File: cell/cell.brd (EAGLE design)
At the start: 35.6 x 48.3 mm, 11 parts

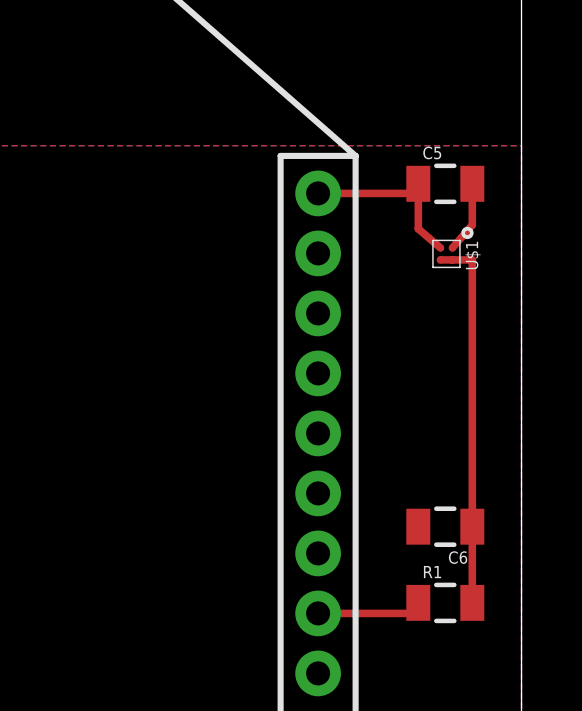
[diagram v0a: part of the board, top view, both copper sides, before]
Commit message: center LMT70 with other chips
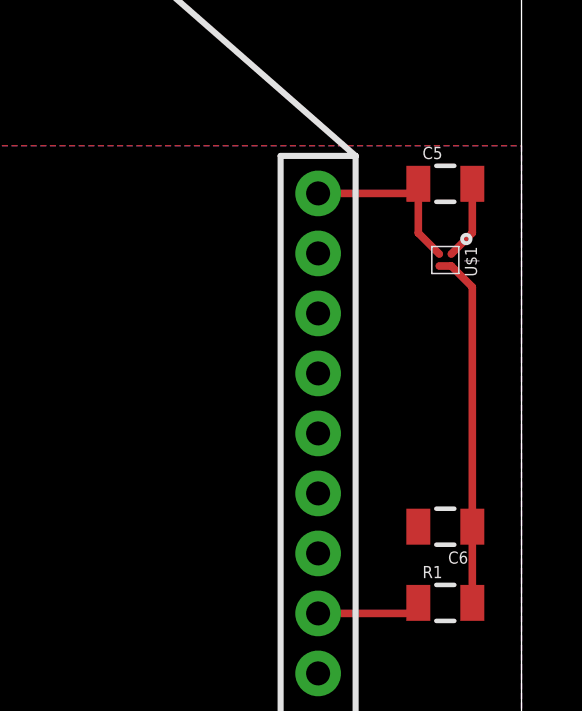
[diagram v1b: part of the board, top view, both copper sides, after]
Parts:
- moved U$1 0.21 mm to (33.0, 30.5)
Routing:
- net N$1: track 12.5 -> 12.0 mm
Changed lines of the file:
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@@
 <element name="C2" library="SparkFun-Capacitors" package="0805" value="1µF" x="25.4" y="6.35"/>
 <element name="XB24" library="hrldcpr" package="XBEE-1" value="XBEE-1XBEE-1" x="17.78" y="12.7"/>
-<element name="U$1" library="lmt40" package="YFP0004" value="LMT40" x="33.0581" y="30.6832" rot="R270"/>
+<element name="U$1" library="lmt40" package="YFP0004" value="LMT40" x="33.02" y="30.48" rot="R270"/>
 </elements>
 <signals>
@@
 <contactref element="XB24" pad="3"/>
 <contactref element="U$1" pad="GND"/>
-<wire x1="33.2581" y1="30.8832" x2="33.92" y2="31.6452" width="0.254" layer="1"/>
-<wire x1="33.92" y1="31.6452" x2="33.92" y2="33.02" width="0.254" layer="1"/>
+<wire x1="33.92" y1="33.02" x2="33.92" y2="31.38" width="0.254" layer="1"/>
+<wire x1="33.92" y1="31.38" x2="33.22" y2="30.68" width="0.254" layer="1"/>
 </signal>
 <signal name="V_BATT">
@@
 <contactref element="U$1" pad="VDD"/>
 <contactref element="U$1" pad="T_ON"/>
-<wire x1="32.8581" y1="30.4832" x2="33.2581" y2="30.4832" width="0.254" layer="1"/>
-<wire x1="33.2581" y1="30.4832" x2="33.92" y2="30.4832" width="0.254" layer="1"/>
-<wire x1="33.92" y1="30.4832" x2="33.92" y2="21.59" width="0.254" layer="1"/>
+<wire x1="32.82" y1="30.28" x2="33.22" y2="30.28" width="0.254" layer="1"/>
+<wire x1="33.22" y1="30.28" x2="33.92" y2="29.58" width="0.254" layer="1"/>
+<wire x1="33.92" y1="29.58" x2="33.92" y2="21.59" width="0.254" layer="1"/>
 </signal>
 <signal name="N$2">
@@
 <wire x1="28.78" y1="32.7" x2="32.12" y2="32.7" width="0.254" layer="1"/>
 <wire x1="32.12" y1="32.7" x2="32.12" y2="33.02" width="0.254" layer="1"/>
-<wire x1="32.8581" y1="30.8832" x2="32.12" y2="31.5182" width="0.254" layer="1"/>
-<wire x1="32.12" y1="31.5182" x2="32.12" y2="33.02" width="0.254" layer="1"/>
+<wire x1="32.12" y1="33.02" x2="32.12" y2="31.38" width="0.254" layer="1"/>
+<wire x1="32.12" y1="31.38" x2="32.82" y2="30.68" width="0.254" layer="1"/>
 </signal>
 </signals>

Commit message: fix LMT70 naming
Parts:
- U$1: value LMT40 -> LMT70; device lmt40:YFP0004 -> lmt70:YFP0004
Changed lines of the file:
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@@
 <element name="C2" library="SparkFun-Capacitors" package="0805" value="1µF" x="25.4" y="6.35"/>
 <element name="XB24" library="hrldcpr" package="XBEE-1" value="XBEE-1XBEE-1" x="17.78" y="12.7"/>
-<element name="U$1" library="lmt40" package="YFP0004" value="LMT40" x="33.02" y="30.48" rot="R270"/>
+<element name="U$1" library="lmt70" package="YFP0004" value="LMT70" x="33.02" y="30.48" rot="R270"/>
 </elements>
 <signals>

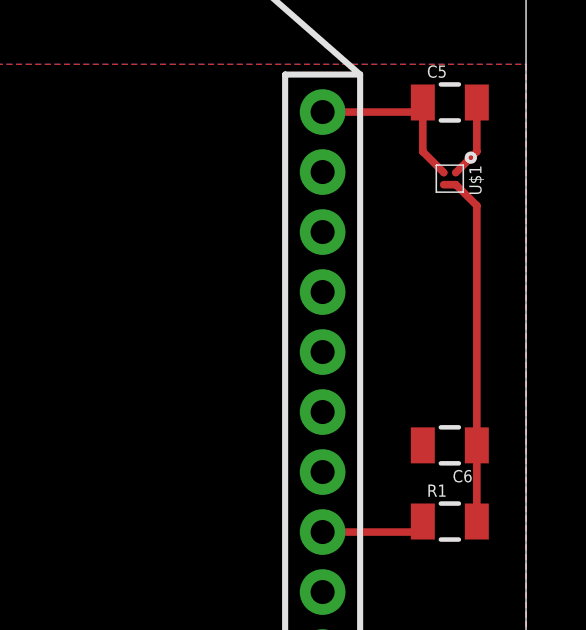
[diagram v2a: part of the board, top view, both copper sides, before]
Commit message: use symmetric traces on BGA chip, to avoid unequal soldering and tension
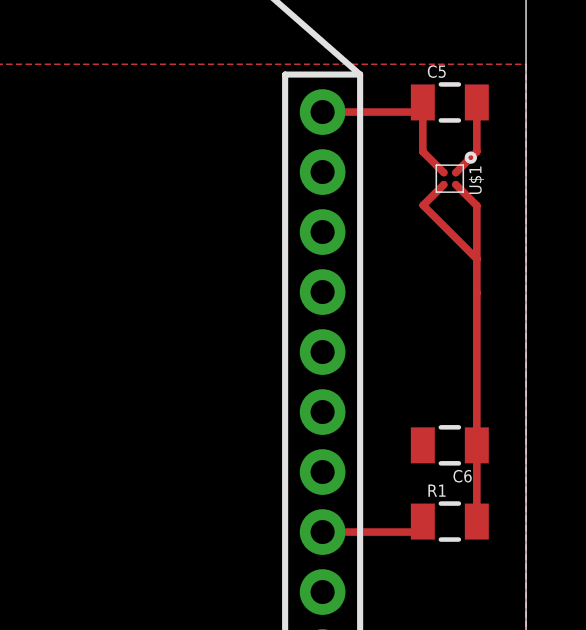
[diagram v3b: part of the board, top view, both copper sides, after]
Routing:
- net N$1: track 12.0 -> 15.1 mm
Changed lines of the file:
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@@
 <contactref element="U$1" pad="VDD"/>
 <contactref element="U$1" pad="T_ON"/>
-<wire x1="32.82" y1="30.28" x2="33.22" y2="30.28" width="0.254" layer="1"/>
 <wire x1="33.22" y1="30.28" x2="33.92" y2="29.58" width="0.254" layer="1"/>
-<wire x1="33.92" y1="29.58" x2="33.92" y2="21.59" width="0.254" layer="1"/>
+<wire x1="33.92" y1="29.58" x2="33.92" y2="27.802" width="0.254" layer="1"/>
+<wire x1="33.92" y1="26.67" x2="33.92" y2="21.59" width="0.254" layer="1"/>
+<wire x1="32.82" y1="30.28" x2="32.131" y2="29.591" width="0.254" layer="1"/>
+<wire x1="32.131" y1="29.591" x2="33.92" y2="27.802" width="0.254" layer="1"/>
+<wire x1="33.92" y1="27.802" x2="33.92" y2="26.67" width="0.254" layer="1"/>
 </signal>
 <signal name="N$2">
